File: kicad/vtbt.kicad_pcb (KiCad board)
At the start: 2 copper layers, 25.4 x 53.3 mm, 35 parts, among them J1 955016449, Q1 MMBT4401, Q2 MMBT4401, Q3 MMBT4401, U1 ESP32-C3-DevKitM-1, U2 LT1032CSW-PBF, U3 MAX3183EEUK+T

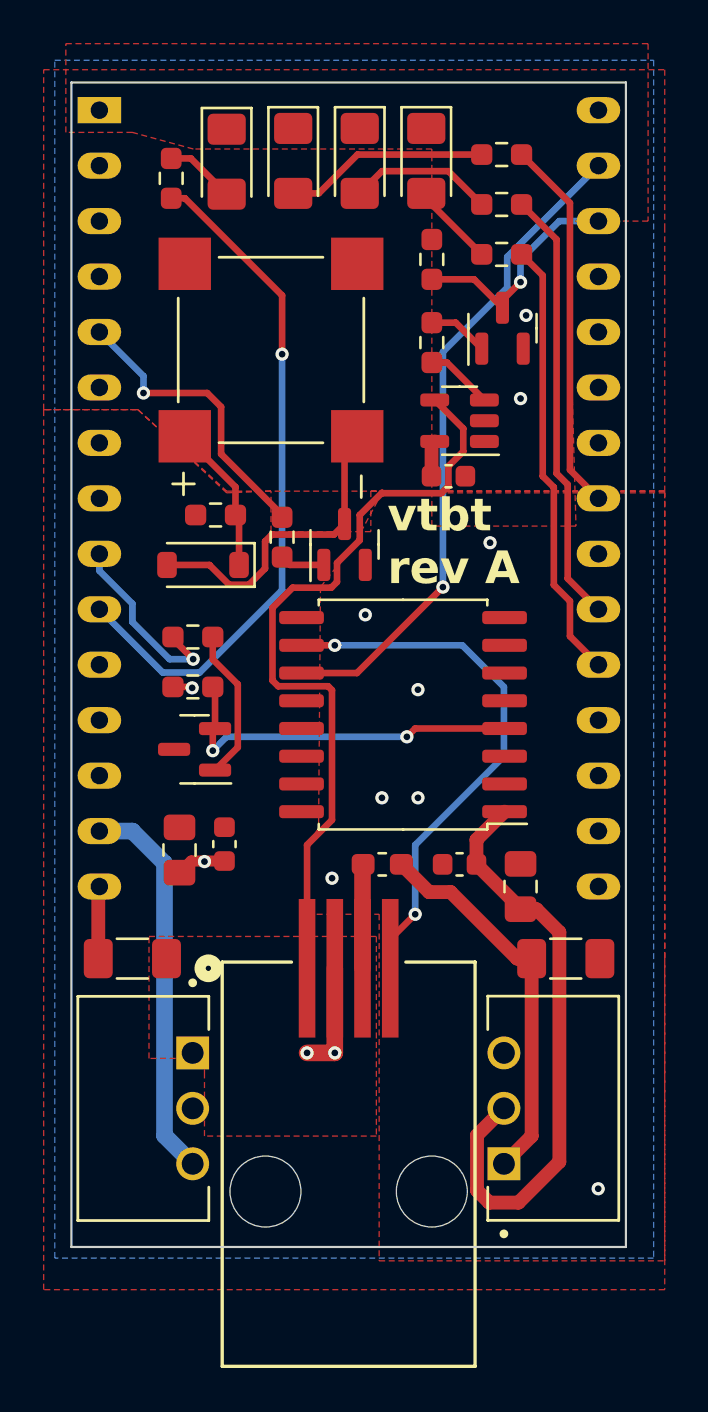
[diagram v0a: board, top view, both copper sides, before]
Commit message: Reroute for rollover-wired modular cable
Phone handset cables are commonly available and use rollover-wiring.
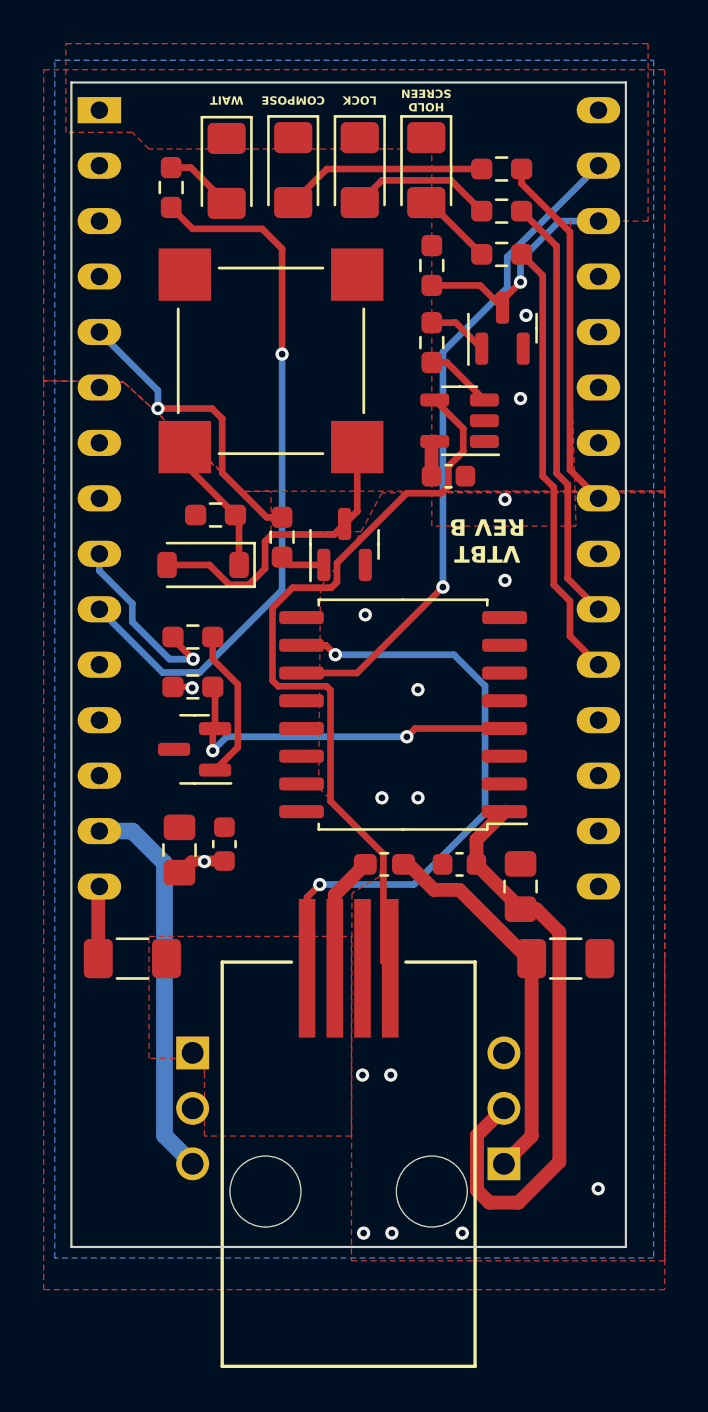
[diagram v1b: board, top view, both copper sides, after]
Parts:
- J1: footprint 955016449:CONN_95501-6449_MOL -> Library:CONN_95501-6449_MOL
- LS1: footprint SMT_0820_S_R:XDCR_SMT-0820-S-R -> Library:XDCR_SMT-0820-S-R
- PS2: footprint PXO7805_500_S:CONV_PXO7805-500-S -> Library:CONV_PXO7805-500-S
- moved R8 0.66 mm to (75.6, 127.2)
- moved LS1 0.50 mm to (65.0, 135.9)
- moved LED0 0.42 mm to (63.0, 127.2)
- moved LED1 0.42 mm to (66.0, 127.2)
- moved LED2 0.42 mm to (69.1, 127.2)
- moved LED3 0.42 mm to (72.1, 127.2)
- moved R5 0.42 mm to (60.5, 128.0)
- moved R7 0.30 mm to (75.6, 129.1)
- moved R9 0.28 mm to (72.4, 131.6)
- moved L1 0.10 mm to (70.2, 159.0)
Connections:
- J1 pad 1: /RS_423_RX -> /RS_423_TX
- J1 pad 2: GND -> +12V
- J1 pad 3: +12V -> GND
- J1 pad 4: /RS_423_TX -> /RS_423_RX
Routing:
- net GND: track 11.6 -> 6.50 mm, vias 13 -> 16
- net /RS_423_TX: track 25.1 -> 28.0 mm
- net /LED0: track 31.6 -> 32.6 mm
- net /LED1: track 17.2 -> 16.5 mm
- net +12V: track 4.77 -> 5.34 mm
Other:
- board text added: "COMPOSE"
- board text added: "HOLD SCREEN"
- board text added: "LOCK"
- board text added: "VTBT REV B"
- board text added: "WAIT"
- board text removed: "vtbt rev A"
